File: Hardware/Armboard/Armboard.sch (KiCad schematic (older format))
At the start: 27 parts

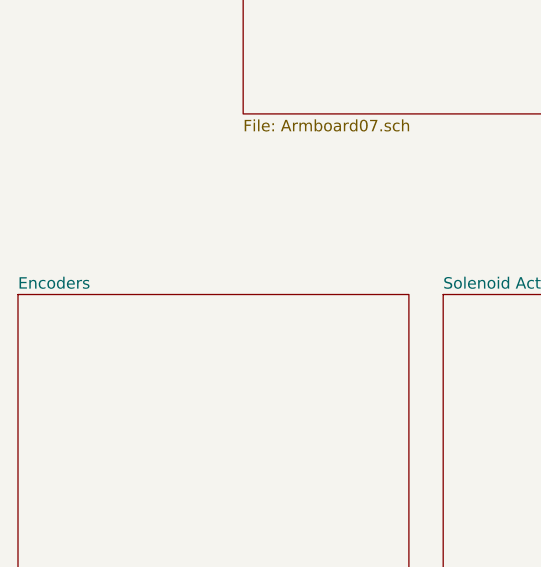
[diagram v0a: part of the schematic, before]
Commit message: Added Software LEDs
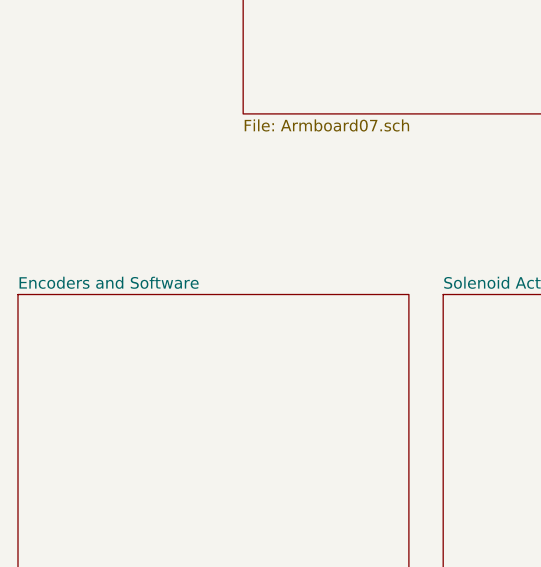
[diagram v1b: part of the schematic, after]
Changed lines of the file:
@@
 S 760  5780 1710 1890
 U 5F738596
-F0 "Encoders" 50
+F0 "Encoders and Software" 50
 F1 "Armboard04.sch" 50
 $EndSheet

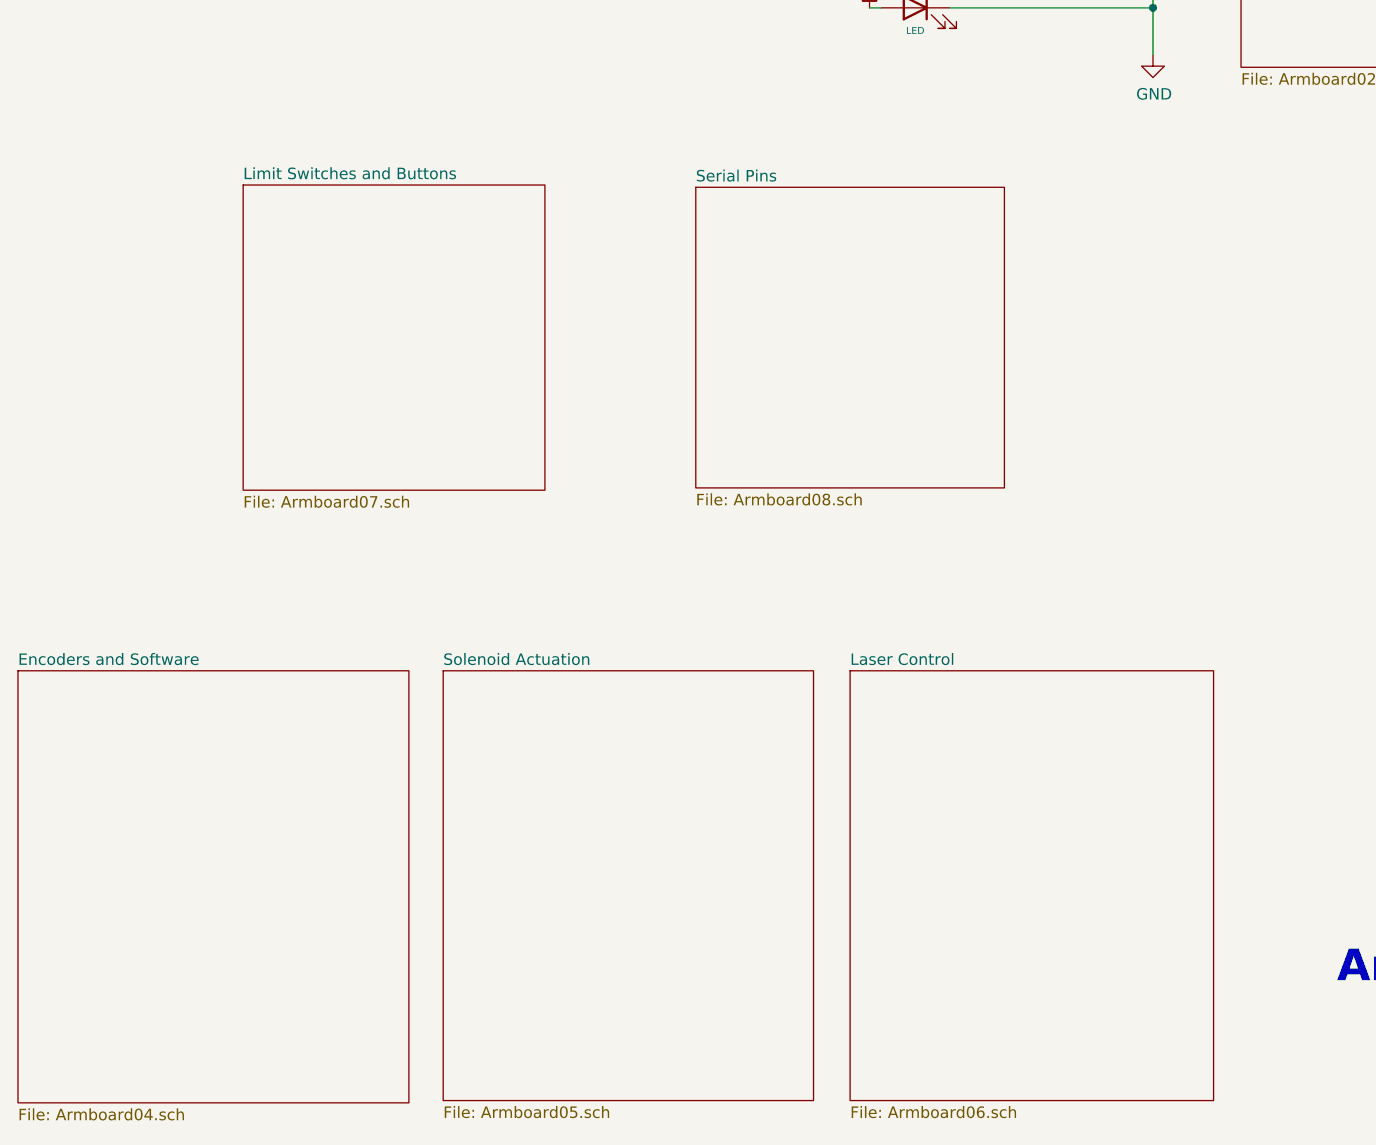
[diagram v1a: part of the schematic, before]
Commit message: Deleted laser and solenoid
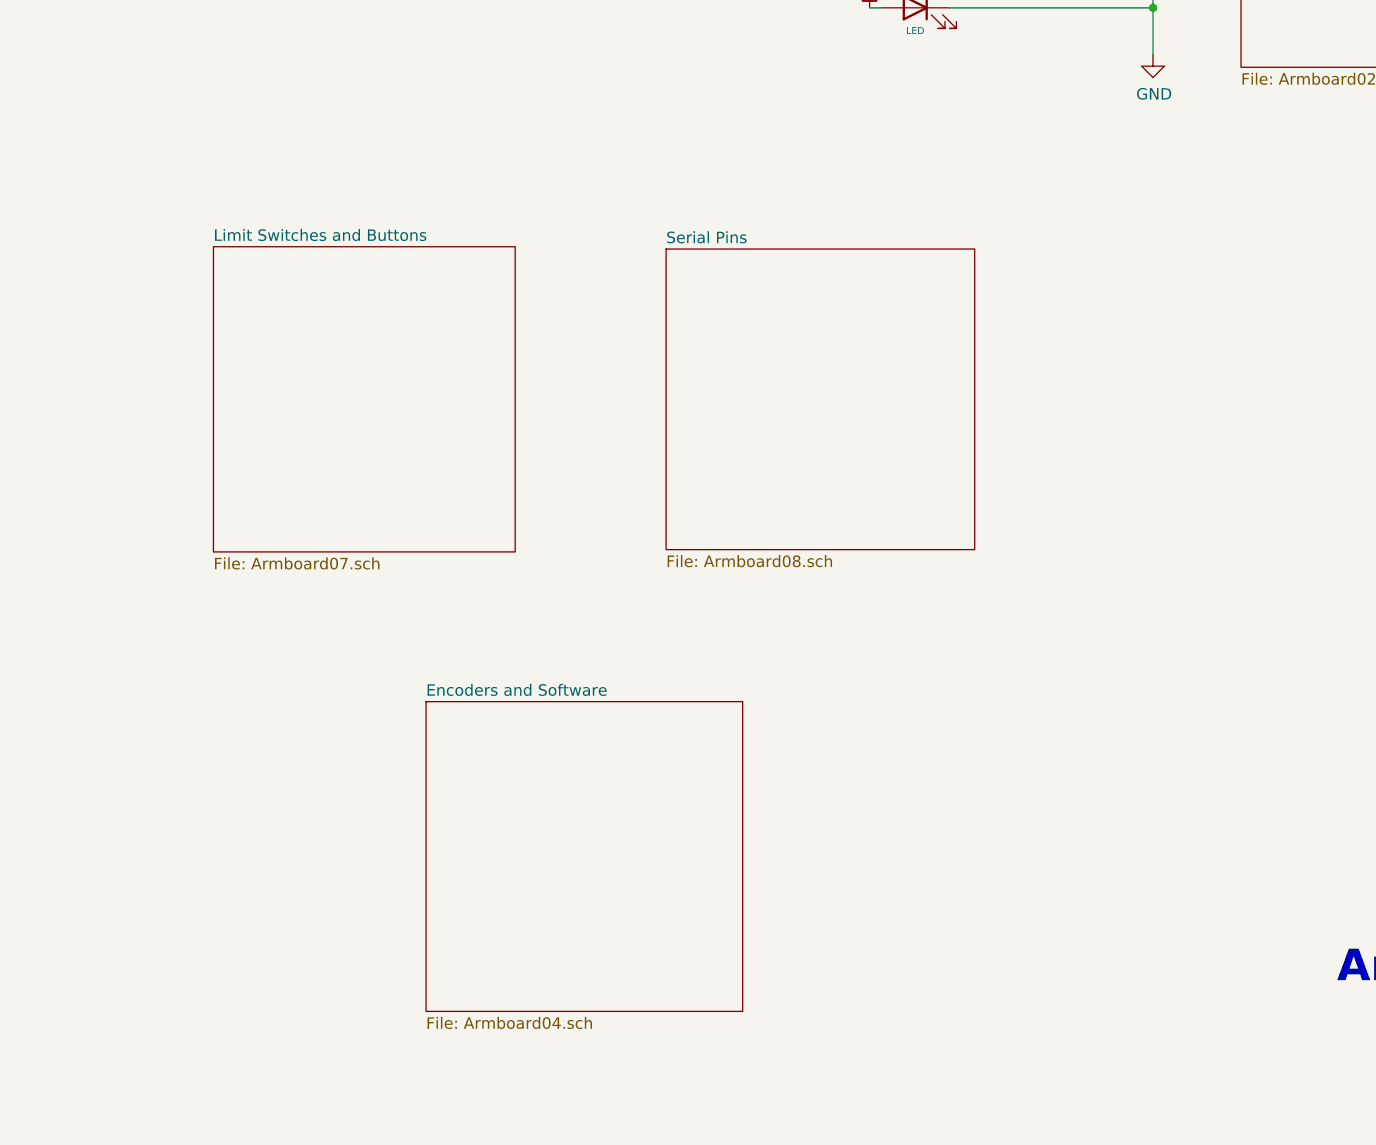
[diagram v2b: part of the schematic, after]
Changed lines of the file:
@@
 $Descr A 11000 8500
 encoding utf-8
-Sheet 1 9
+Sheet 1 7
 Title ""
 Date ""
@@
 $EndSheet
 $Sheet
-S 760  5780 1710 1890
+S 2545 5915 1385 1355
 U 5F738596
 F0 "Encoders and Software" 50
@@
 $EndSheet
 $Sheet
-S 2620 5780 1620 1880
-U 5F738767
-F0 "Solenoid Actuation" 50
-F1 "Armboard05.sch" 50
-$EndSheet
-$Sheet
-S 4400 5780 1590 1880
-U 5F73890D
-F0 "Laser Control" 50
-F1 "Armboard06.sch" 50
-$EndSheet
-$Sheet
-S 1745 3655 1320 1335
+S 1615 3925 1320 1335
 U 5F739ECE
 F0 "Limit Switches and Buttons" 50
@@
 $EndSheet
 $Sheet
-S 3725 3665 1350 1315
+S 3595 3935 1350 1315
 U 5F73A06A
 F0 "Serial Pins" 50

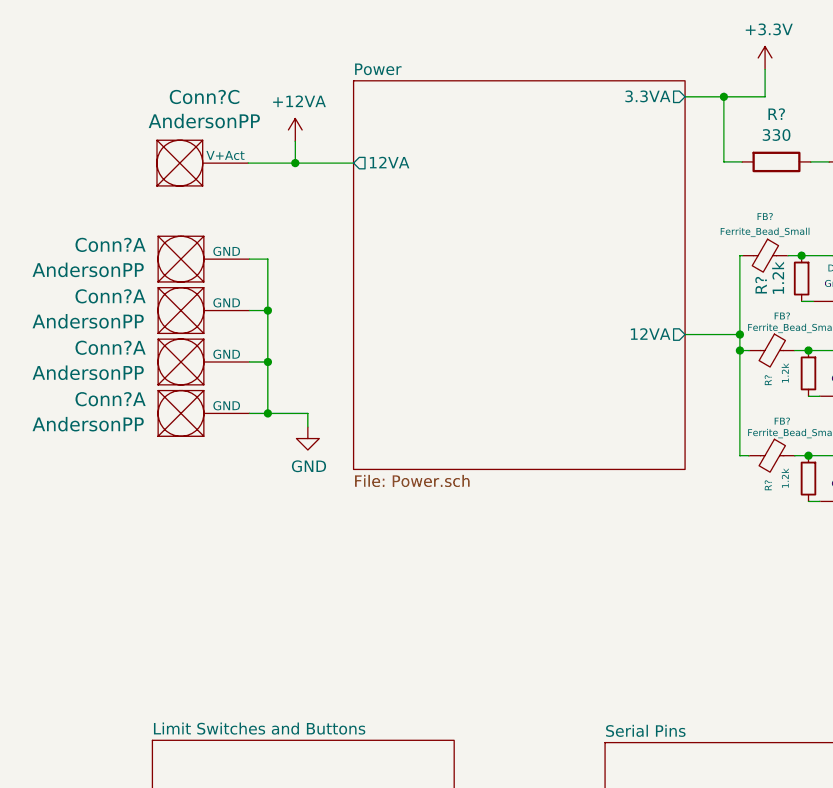
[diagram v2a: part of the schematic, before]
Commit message: Attempted to add 12 VL line
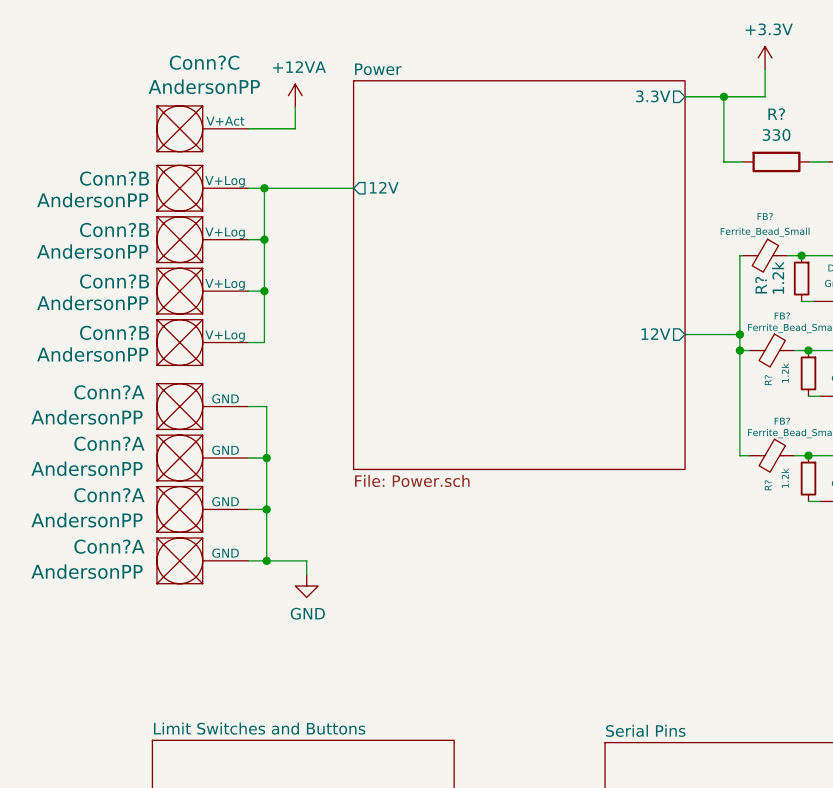
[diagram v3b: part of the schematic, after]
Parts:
- added Conn? (x4): AndersonPP, symbol MRDT_Connectors:AndersonPP
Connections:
- net Power/12VA renamed Power/12V
- new net Power/12V: Conn?.2 (V+Log), Conn?.2 (V+Log), Conn?.2 (V+Log), Conn?.2 (V+Log)
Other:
- moved on the sheet: Conn?A, Conn?C
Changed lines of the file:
@@
 F0 "Power" 50
 F1 "Power.sch" 50
-F2 "3.3VA" O R 3945 1110 50
-F3 "12VA" O R 3945 2150 50
-F4 "12VA" O L 2495 1400 50
+F2 "3.3V" O R 3945 1110 50
+F3 "12V" O R 3945 2150 50
+F4 "12V" O L 2495 1510 50
 $EndSheet
 $Comp
 L power:GND #PWR?
 U 1 1 5F73C160
-P 2295 2555
+P 2290 3200
 AR Path="/5F67ABAC/5F73C160" Ref="#PWR?"  Part="1"
 AR Path="/5F73C160" Ref="#PWR?"  Part="1"
-F 0 "#PWR?" H 2295 2305 50  0001 C CNN
-F 1 "GND" H 2300 2382 50  0000 C CNN
-F 2 "" H 2295 2555 50  0001 C CNN
-F 3 "" H 2295 2555 50  0001 C CNN
-	1    2295 2555
+F 0 "#PWR?" H 2290 2950 50  0001 C CNN
+F 1 "GND" H 2295 3027 50  0000 C CNN
+F 2 "" H 2290 3200 50  0001 C CNN
+F 3 "" H 2290 3200 50  0001 C CNN
+	1    2290 3200
 	1    0    0    -1
 $EndComp
@@
 L Armboard-rescue:AndersonPP-MRDT_Connectors-Armboard-rescue-Armboard-rescue-Armboard-rescue Conn?
 U 3 1 5F742EAC
-P 1635 1500
+P 1635 1350
 AR Path="/5F742EAC" Ref="Conn?"  Part="3"
 AR Path="/5F67ABAC/5F742EAC" Ref="Conn?"  Part="3"
-F 0 "Conn?" H 1843 1887 60  0000 C CNN
-F 1 "AndersonPP" H 1843 1781 60  0000 C CNN
-F 2 "" H 1485 950 60  0001 C CNN
-F 3 "" H 1485 950 60  0001 C CNN
-	3    1635 1500
+F 0 "Conn?" H 1843 1737 60  0000 C CNN
+F 1 "AndersonPP" H 1843 1631 60  0000 C CNN
+F 2 "" H 1485 800 60  0001 C CNN
+F 3 "" H 1485 800 60  0001 C CNN
+	3    1635 1350
 	1    0    0    -1
 $EndComp
@@
 $EndComp
 Wire Wire Line
-	2035 1400 2240 1400
+	2035 1250 2240 1250
 $Comp
 L MRDT_Connectors:AndersonPP Conn?
 U 1 1 5F89DF6A
-P 1640 2145
-F 0 "Conn?" H 1430 2305 60  0000 C CNN
-F 1 "AndersonPP" H 1335 2195 60  0000 C CNN
-F 2 "" H 1490 1595 60  0001 C CNN
-F 3 "" H 1490 1595 60  0001 C CNN
-	1    1640 2145
+P 1635 2790
+F 0 "Conn?" H 1425 2950 60  0000 C CNN
+F 1 "AndersonPP" H 1330 2840 60  0000 C CNN
+F 2 "" H 1485 2240 60  0001 C CNN
+F 3 "" H 1485 2240 60  0001 C CNN
+	1    1635 2790
 	1    0    0    -1
 $EndComp
@@
 L MRDT_Connectors:AndersonPP Conn?
 U 1 1 5F89F797
-P 1640 2370
-F 0 "Conn?" H 1430 2530 60  0000 C CNN
-F 1 "AndersonPP" H 1335 2420 60  0000 C CNN
-F 2 "" H 1490 1820 60  0001 C CNN
-F 3 "" H 1490 1820 60  0001 C CNN
-	1    1640 2370
+P 1635 3015
+F 0 "Conn?" H 1425 3175 60  0000 C CNN
+F 1 "AndersonPP" H 1330 3065 60  0000 C CNN
+F 2 "" H 1485 2465 60  0001 C CNN
+F 3 "" H 1485 2465 60  0001 C CNN
+	1    1635 3015
 	1    0    0    -1
 $EndComp
@@
 L MRDT_Connectors:AndersonPP Conn?
 U 1 1 5F8A00CD
-P 1640 2595
-F 0 "Conn?" H 1430 2755 60  0000 C CNN
-F 1 "AndersonPP" H 1335 2645 60  0000 C CNN
-F 2 "" H 1490 2045 60  0001 C CNN
-F 3 "" H 1490 2045 60  0001 C CNN
-	1    1640 2595
+P 1635 3240
+F 0 "Conn?" H 1425 3400 60  0000 C CNN
+F 1 "AndersonPP" H 1330 3290 60  0000 C CNN
+F 2 "" H 1485 2690 60  0001 C CNN
+F 3 "" H 1485 2690 60  0001 C CNN
+	1    1635 3240
 	1    0    0    -1
 $EndComp
@@
 L MRDT_Connectors:AndersonPP Conn?
 U 1 1 5F8A3390
-P 1640 1920
-F 0 "Conn?" H 1430 2080 60  0000 C CNN
-F 1 "AndersonPP" H 1335 1970 60  0000 C CNN
-F 2 "" H 1490 1370 60  0001 C CNN
-F 3 "" H 1490 1370 60  0001 C CNN
-	1    1640 1920
-	1    0    0    -1
-$EndComp
-Wire Wire Line
-	2040 1820 2120 1820
-Wire Wire Line
-	2120 2495 2040 2495
-Wire Wire Line
-	2295 2555 2295 2495
-Wire Wire Line
-	2295 2495 2120 2495
-Connection ~ 2120 2495
-Wire Wire Line
-	2040 2270 2120 2270
-Connection ~ 2120 2270
-Wire Wire Line
-	2120 2270 2120 2495
-Wire Wire Line
-	2040 2045 2120 2045
-Wire Wire Line
-	2120 1820 2120 2045
-Connection ~ 2120 2045
-Wire Wire Line
-	2120 2045 2120 2270
+P 1635 2565
+F 0 "Conn?" H 1425 2725 60  0000 C CNN
+F 1 "AndersonPP" H 1330 2615 60  0000 C CNN
+F 2 "" H 1485 2015 60  0001 C CNN
+F 3 "" H 1485 2015 60  0001 C CNN
+	1    1635 2565
+	1    0    0    -1
+$EndComp
+Wire Wire Line
+	2035 2465 2115 2465
+Wire Wire Line
+	2115 3140 2035 3140
+Wire Wire Line
+	2290 3200 2290 3140
+Wire Wire Line
+	2290 3140 2115 3140
+Connection ~ 2115 3140
+Wire Wire Line
+	2035 2915 2115 2915
+Connection ~ 2115 2915
+Wire Wire Line
+	2115 2915 2115 3140
+Wire Wire Line
+	2035 2690 2115 2690
+Wire Wire Line
+	2115 2465 2115 2690
+Connection ~ 2115 2690
+Wire Wire Line
+	2115 2690 2115 2915
 $Comp
 L Device:Ferrite_Bead_Small FB?
@@
 L power:+12VA #PWR?
 U 1 1 5F9AAE95
-P 2240 1305
-F 0 "#PWR?" H 2240 1155 50  0001 C CNN
-F 1 "+12VA" H 2255 1478 50  0000 C CNN
-F 2 "" H 2240 1305 50  0001 C CNN
-F 3 "" H 2240 1305 50  0001 C CNN
-	1    2240 1305
-	1    0    0    -1
-$EndComp
-Wire Wire Line
-	2240 1305 2240 1400
-Connection ~ 2240 1400
-Wire Wire Line
-	2240 1400 2495 1400
+P 2240 1155
+F 0 "#PWR?" H 2240 1005 50  0001 C CNN
+F 1 "+12VA" H 2255 1328 50  0000 C CNN
+F 2 "" H 2240 1155 50  0001 C CNN
+F 3 "" H 2240 1155 50  0001 C CNN
+	1    2240 1155
+	1    0    0    -1
+$EndComp
+Wire Wire Line
+	2240 1155 2240 1250
 $Comp
 L Device:Ferrite_Bead_Small FB?
@@
 Wire Wire Line
 	5725 2880 5725 3085
+$Comp
+L MRDT_Connectors:AndersonPP Conn?
+U 2 1 5FAB26A6
+P 1635 1610
+F 0 "Conn?" H 1450 1750 60  0000 C CNN
+F 1 "AndersonPP" H 1355 1655 60  0000 C CNN
+F 2 "" H 1485 1060 60  0001 C CNN
+F 3 "" H 1485 1060 60  0001 C CNN
+	2    1635 1610
+	1    0    0    -1
+$EndComp
+Wire Wire Line
+	2035 1510 2105 1510
+$Comp
+L MRDT_Connectors:AndersonPP Conn?
+U 2 1 5FAC069B
+P 1635 1835
+F 0 "Conn?" H 1450 1975 60  0000 C CNN
+F 1 "AndersonPP" H 1355 1880 60  0000 C CNN
+F 2 "" H 1485 1285 60  0001 C CNN
+F 3 "" H 1485 1285 60  0001 C CNN
+	2    1635 1835
+	1    0    0    -1
+$EndComp
+$Comp
+L MRDT_Connectors:AndersonPP Conn?
+U 2 1 5FAC17F9
+P 1635 2060
+F 0 "Conn?" H 1450 2200 60  0000 C CNN
+F 1 "AndersonPP" H 1355 2105 60  0000 C CNN
+F 2 "" H 1485 1510 60  0001 C CNN
+F 3 "" H 1485 1510 60  0001 C CNN
+	2    1635 2060
+	1    0    0    -1
+$EndComp
+$Comp
+L MRDT_Connectors:AndersonPP Conn?
+U 2 1 5FAC298C
+P 1635 2285
+F 0 "Conn?" H 1450 2425 60  0000 C CNN
+F 1 "AndersonPP" H 1355 2330 60  0000 C CNN
+F 2 "" H 1485 1735 60  0001 C CNN
+F 3 "" H 1485 1735 60  0001 C CNN
+	2    1635 2285
+	1    0    0    -1
+$EndComp
+Wire Wire Line
+	2035 2185 2105 2185
+Wire Wire Line
+	2105 2185 2105 1960
+Connection ~ 2105 1510
+Wire Wire Line
+	2105 1510 2495 1510
+Wire Wire Line
+	2035 1960 2105 1960
+Connection ~ 2105 1960
+Wire Wire Line
+	2105 1960 2105 1735
+Wire Wire Line
+	2035 1735 2105 1735
+Connection ~ 2105 1735
+Wire Wire Line
+	2105 1735 2105 1510
 $EndSCHEMATC

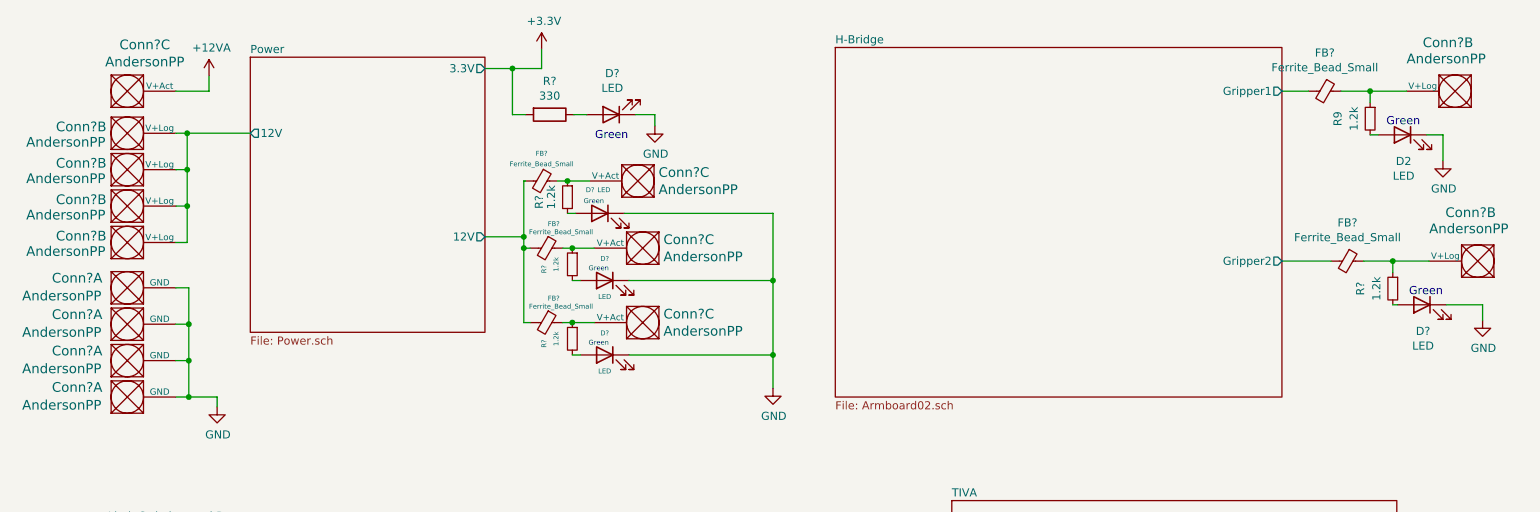
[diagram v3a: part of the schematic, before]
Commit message: Assigned R/L/C footprints
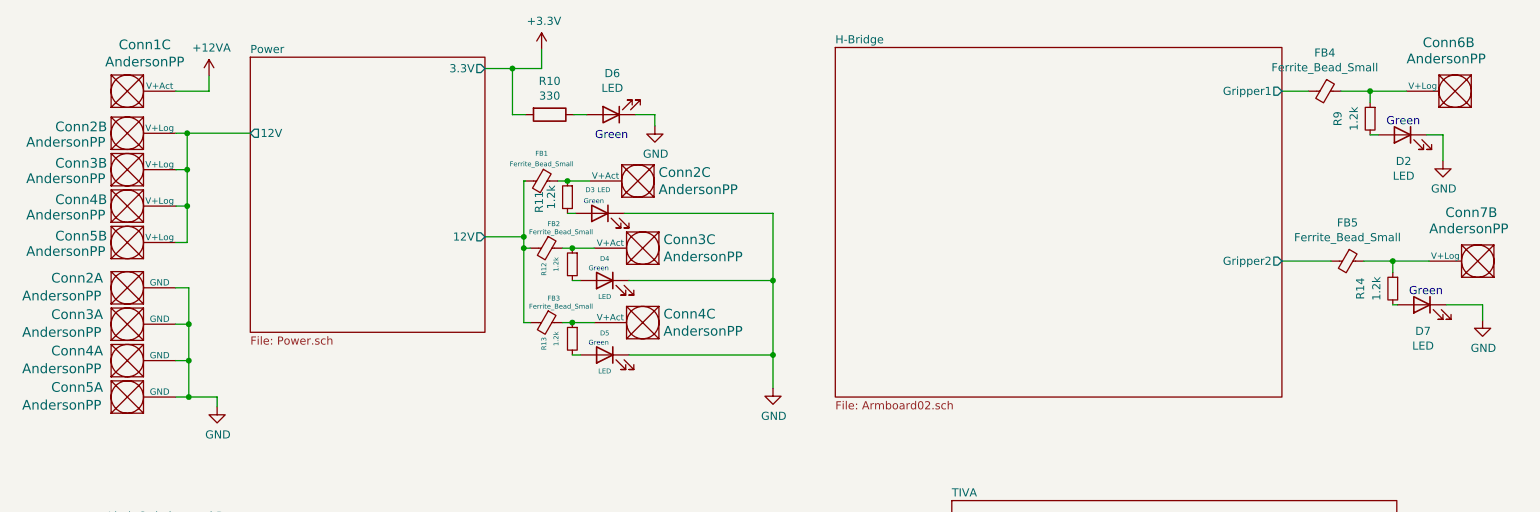
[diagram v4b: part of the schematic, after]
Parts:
- R10, R11, R12, R13, R14: renamed from R?; footprint (none) -> Resistor_SMD:R_0603_1608Metric_Pad1.05x0.95mm_HandSolder
- R9: footprint (none) -> Resistor_SMD:R_0603_1608Metric_Pad1.05x0.95mm_HandSolder
- gave numbers to parts that had none: 17
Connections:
- net Power/12V is gone; now on net Power/12V: Conn2.2 (V+Log), Conn3.2 (V+Log), Conn4.2 (V+Log), Conn5.2 (V+Log)
- net Power/12V: no longer FB1.2, FB2.2, FB3.2
- new net Power/12V: FB1.2, FB2.2, FB3.2
